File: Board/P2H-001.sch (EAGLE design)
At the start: 26 parts, among them IC1 LTC485N, IC2 74LS07N, IC3 74LS157N, IC4 LTC485N, IC5 TLC5941NT, U1 ARDUINO_PRO_MINI

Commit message: Brush up.
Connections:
- net GND: now also CN2.4
- net VCC: now also CN2.1; no longer CN2.4
- net VDD: no longer CN2.1
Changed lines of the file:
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@@
 <part name="SUPPLY32" library="supply2" deviceset="VCC" device=""/>
 <part name="JP1" library="pinhead" deviceset="PINHD-1X2" device=""/>
-<part name="VDD1" library="supply1" deviceset="VDD" device=""/>
 <part name="SUPPLY15" library="supply2" deviceset="VCC" device=""/>
 <part name="SUPPLY13" library="supply2" deviceset="GND" device=""/>
@@
 <instance part="SUPPLY32" gate="G$1" x="243.84" y="-50.8"/>
 <instance part="JP1" gate="G$1" x="33.02" y="-38.1"/>
-<instance part="VDD1" gate="G$1" x="27.94" y="134.62"/>
 <instance part="SUPPLY15" gate="G$1" x="167.64" y="127"/>
 <instance part="SUPPLY13" gate="GND" x="147.32" y="-22.86"/>
@@
 <pinref part="CN2" gate="G$1" pin="2"/>
 <pinref part="CN2" gate="G$1" pin="3"/>
+<pinref part="CN2" gate="G$1" pin="4"/>
+<wire x1="5.08" y1="38.1" x2="12.7" y2="38.1" width="0.1524" layer="91"/>
+<wire x1="12.7" y1="38.1" x2="12.7" y2="35.56" width="0.1524" layer="91"/>
+<junction x="12.7" y="35.56"/>
 </segment>
 <segment>
@@
 <segment>
 <pinref part="SUPPLY2" gate="G$1" pin="VCC"/>
-<wire x1="25.4" y1="38.1" x2="25.4" y2="124.46" width="0.1524" layer="91"/>
-<wire x1="25.4" y1="38.1" x2="5.08" y2="38.1" width="0.1524" layer="91"/>
-<pinref part="CN2" gate="G$1" pin="4"/>
+<wire x1="25.4" y1="30.48" x2="25.4" y2="124.46" width="0.1524" layer="91"/>
+<pinref part="CN2" gate="G$1" pin="1"/>
+<wire x1="25.4" y1="30.48" x2="5.08" y2="30.48" width="0.1524" layer="91"/>
 </segment>
 <segment>
@@
 <wire x1="254" y1="15.24" x2="261.62" y2="15.24" width="0.1524" layer="91"/>
 <pinref part="SV2" gate="G$1" pin="6"/>
+<label x="218.44" y="-7.62" size="1.778" layer="95"/>
 </segment>
 </net>
@@
 <wire x1="251.46" y1="17.78" x2="251.46" y2="-10.16" width="0.1524" layer="91"/>
 <pinref part="SV2" gate="G$1" pin="8"/>
+<label x="218.44" y="-10.16" size="1.778" layer="95"/>
 </segment>
 </net>
@@
 <wire x1="284.48" y1="15.24" x2="276.86" y2="15.24" width="0.1524" layer="91"/>
 <pinref part="SV2" gate="G$1" pin="5"/>
+<label x="218.44" y="-15.24" size="1.778" layer="95"/>
 </segment>
 </net>
@@
 <wire x1="256.54" y1="12.7" x2="256.54" y2="-2.54" width="0.1524" layer="91"/>
 <pinref part="SV2" gate="G$1" pin="4"/>
+<label x="218.44" y="-2.54" size="1.778" layer="95"/>
 </segment>
 </net>
@@
 <wire x1="281.94" y1="12.7" x2="276.86" y2="12.7" width="0.1524" layer="91"/>
 <pinref part="SV2" gate="G$1" pin="3"/>
+<label x="218.44" y="-5.08" size="1.778" layer="95"/>
 </segment>
 </net>
@@
 <wire x1="116.84" y1="45.72" x2="116.84" y2="132.08" width="0.1524" layer="91"/>
 <pinref part="U1" gate="G$1" pin="RAW"/>
-</segment>
-<segment>
-<pinref part="VDD1" gate="G$1" pin="VDD"/>
-<wire x1="27.94" y1="132.08" x2="27.94" y2="30.48" width="0.1524" layer="91"/>
-<wire x1="27.94" y1="30.48" x2="5.08" y2="30.48" width="0.1524" layer="91"/>
-<pinref part="CN2" gate="G$1" pin="1"/>
 </segment>
 <segment>
@@
 <wire x1="287.02" y1="17.78" x2="276.86" y2="17.78" width="0.1524" layer="91"/>
 <pinref part="SV2" gate="G$1" pin="7"/>
-</segment>
-</net>
+<label x="218.44" y="-12.7" size="1.778" layer="95"/>
+</segment>
+</net>

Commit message: Hotfix.
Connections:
- new net N$10: IC5.SOUT, SV2.3
- net SIN: no longer SV2.3
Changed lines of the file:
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@@
 <wire x1="114.3" y1="20.32" x2="109.22" y2="20.32" width="0.1524" layer="91"/>
 <label x="111.76" y="20.32" size="1.778" layer="95"/>
-<wire x1="215.9" y1="-5.08" x2="281.94" y2="-5.08" width="0.1524" layer="91"/>
-<junction x="215.9" y="-5.08"/>
 <pinref part="U1" gate="G$1" pin="*11"/>
-<wire x1="281.94" y1="-5.08" x2="281.94" y2="12.7" width="0.1524" layer="91"/>
-<wire x1="281.94" y1="12.7" x2="276.86" y2="12.7" width="0.1524" layer="91"/>
-<pinref part="SV2" gate="G$1" pin="3"/>
 <label x="218.44" y="-5.08" size="1.778" layer="95"/>
 </segment>
@@
 </segment>
 </net>
+<net name="N$10" class="0">
+<segment>
+<pinref part="SV2" gate="G$1" pin="3"/>
+<wire x1="281.94" y1="12.7" x2="276.86" y2="12.7" width="0.1524" layer="91"/>
+<pinref part="IC5" gate="G$1" pin="SOUT"/>
+<wire x1="218.44" y1="7.62" x2="218.44" y2="2.54" width="0.1524" layer="91"/>
+<wire x1="218.44" y1="2.54" x2="281.94" y2="2.54" width="0.1524" layer="91"/>
+<wire x1="281.94" y1="2.54" x2="281.94" y2="12.7" width="0.1524" layer="91"/>
+</segment>
+</net>

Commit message: Board and Doc update.
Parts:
- added JP2: (no value), pinhead:PINHD-1X2
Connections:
- net MIDIRX: now also JP2.2
- net N$1: now also JP2.1
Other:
- moved on the sheet: JP1
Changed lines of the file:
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@@
 <part name="VDD5" library="supply1" deviceset="VDD" device=""/>
 <part name="SV2" library="con-ml" deviceset="ML10" device=""/>
+<part name="JP2" library="pinhead" deviceset="PINHD-1X2" device=""/>
 </parts>
 <sheets>
@@
 <instance part="SUPPLY29" gate="G$1" x="236.22" y="-50.8"/>
 <instance part="SUPPLY32" gate="G$1" x="243.84" y="-50.8"/>
-<instance part="JP1" gate="G$1" x="33.02" y="-38.1"/>
+<instance part="JP1" gate="G$1" x="40.64" y="-12.7"/>
 <instance part="SUPPLY15" gate="G$1" x="167.64" y="127"/>
 <instance part="SUPPLY13" gate="GND" x="147.32" y="-22.86"/>
@@
 <instance part="VDD5" gate="G$1" x="281.94" y="33.02"/>
 <instance part="SV2" gate="G$1" x="269.24" y="15.24"/>
+<instance part="JP2" gate="G$1" x="88.9" y="-30.48"/>
 </instances>
 <busses>
@@
 <label x="116.84" y="-60.96" size="1.778" layer="95"/>
 <pinref part="IC3" gate="A" pin="1A"/>
-<wire x1="58.42" y1="-60.96" x2="152.4" y2="-60.96" width="0.1524" layer="91"/>
+<wire x1="58.42" y1="-60.96" x2="78.74" y2="-60.96" width="0.1524" layer="91"/>
+<pinref part="JP2" gate="G$1" pin="2"/>
+<wire x1="78.74" y1="-60.96" x2="152.4" y2="-60.96" width="0.1524" layer="91"/>
+<wire x1="86.36" y1="-30.48" x2="78.74" y2="-30.48" width="0.1524" layer="91"/>
+<wire x1="78.74" y1="-30.48" x2="78.74" y2="-60.96" width="0.1524" layer="91"/>
+<junction x="78.74" y="-60.96"/>
 </segment>
 </net>
@@
 <net name="RX" class="0">
 <segment>
-<pinref part="JP1" gate="G$1" pin="1"/>
-<wire x1="30.48" y1="-35.56" x2="30.48" y2="43.18" width="0.1524" layer="91"/>
 <wire x1="30.48" y1="43.18" x2="86.36" y2="43.18" width="0.1524" layer="91"/>
 <label x="76.2" y="43.18" size="1.778" layer="95"/>
 <pinref part="U1" gate="G$1" pin="RXI"/>
+<pinref part="JP1" gate="G$1" pin="1"/>
+<wire x1="30.48" y1="43.18" x2="30.48" y2="-10.16" width="0.1524" layer="91"/>
+<wire x1="30.48" y1="-10.16" x2="38.1" y2="-10.16" width="0.1524" layer="91"/>
 </segment>
 </net>
@@
 <segment>
 <pinref part="JP1" gate="G$1" pin="2"/>
-<wire x1="30.48" y1="-38.1" x2="30.48" y2="-60.96" width="0.1524" layer="91"/>
+<wire x1="38.1" y1="-12.7" x2="30.48" y2="-12.7" width="0.1524" layer="91"/>
+<wire x1="30.48" y1="-12.7" x2="30.48" y2="-27.94" width="0.1524" layer="91"/>
 <pinref part="IC3" gate="A" pin="1Y"/>
+<wire x1="30.48" y1="-27.94" x2="30.48" y2="-60.96" width="0.1524" layer="91"/>
 <wire x1="33.02" y1="-60.96" x2="30.48" y2="-60.96" width="0.1524" layer="91"/>
-</segment>
-</net>
+<pinref part="JP2" gate="G$1" pin="1"/>
+<wire x1="86.36" y1="-27.94" x2="30.48" y2="-27.94" width="0.1524" layer="91"/>
+<junction x="30.48" y="-27.94"/>
+</segment>
+</net>

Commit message: Jumper to Switch.
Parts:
- removed JP1, JP2: (no value), pinhead:PINHD-1X2
- added S1: TL39PO, switch:TL39PO
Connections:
- net MIDIRX: now also S1.O; no longer JP2.2
- net N$1: now also S1.S; no longer JP1.2, JP2.1
- net RX: now also S1.P; no longer JP1.1
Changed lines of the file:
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@@
 <part name="SUPPLY29" library="supply2" deviceset="VCC" device=""/>
 <part name="SUPPLY32" library="supply2" deviceset="VCC" device=""/>
-<part name="JP1" library="pinhead" deviceset="PINHD-1X2" device=""/>
 <part name="SUPPLY15" library="supply2" deviceset="VCC" device=""/>
 <part name="SUPPLY13" library="supply2" deviceset="GND" device=""/>
@@
 <part name="VDD5" library="supply1" deviceset="VDD" device=""/>
 <part name="SV2" library="con-ml" deviceset="ML10" device=""/>
-<part name="JP2" library="pinhead" deviceset="PINHD-1X2" device=""/>
+<part name="S1" library="switch" deviceset="TL39PO" device=""/>
 </parts>
 <sheets>
@@
 <instance part="SUPPLY29" gate="G$1" x="236.22" y="-50.8"/>
 <instance part="SUPPLY32" gate="G$1" x="243.84" y="-50.8"/>
-<instance part="JP1" gate="G$1" x="40.64" y="-12.7"/>
 <instance part="SUPPLY15" gate="G$1" x="167.64" y="127"/>
 <instance part="SUPPLY13" gate="GND" x="147.32" y="-22.86"/>
@@
 <instance part="VDD5" gate="G$1" x="281.94" y="33.02"/>
 <instance part="SV2" gate="G$1" x="269.24" y="15.24"/>
-<instance part="JP2" gate="G$1" x="88.9" y="-30.48"/>
+<instance part="S1" gate="BEF1" x="33.02" y="-7.62" rot="R180"/>
 </instances>
 <busses>
@@
 <pinref part="IC3" gate="A" pin="1A"/>
 <wire x1="58.42" y1="-60.96" x2="78.74" y2="-60.96" width="0.1524" layer="91"/>
-<pinref part="JP2" gate="G$1" pin="2"/>
 <wire x1="78.74" y1="-60.96" x2="152.4" y2="-60.96" width="0.1524" layer="91"/>
-<wire x1="86.36" y1="-30.48" x2="78.74" y2="-30.48" width="0.1524" layer="91"/>
 <wire x1="78.74" y1="-30.48" x2="78.74" y2="-60.96" width="0.1524" layer="91"/>
 <junction x="78.74" y="-60.96"/>
+<pinref part="S1" gate="BEF1" pin="O"/>
+<wire x1="35.56" y1="-12.7" x2="35.56" y2="-30.48" width="0.1524" layer="91"/>
+<wire x1="35.56" y1="-30.48" x2="78.74" y2="-30.48" width="0.1524" layer="91"/>
+<label x="35.56" y="-22.86" size="1.778" layer="95"/>
 </segment>
 </net>
@@
 <net name="RX" class="0">
 <segment>
-<wire x1="30.48" y1="43.18" x2="86.36" y2="43.18" width="0.1524" layer="91"/>
 <label x="76.2" y="43.18" size="1.778" layer="95"/>
 <pinref part="U1" gate="G$1" pin="RXI"/>
-<pinref part="JP1" gate="G$1" pin="1"/>
-<wire x1="30.48" y1="43.18" x2="30.48" y2="-10.16" width="0.1524" layer="91"/>
-<wire x1="30.48" y1="-10.16" x2="38.1" y2="-10.16" width="0.1524" layer="91"/>
+<pinref part="S1" gate="BEF1" pin="P"/>
+<wire x1="33.02" y1="43.18" x2="86.36" y2="43.18" width="0.1524" layer="91"/>
+<wire x1="33.02" y1="-2.54" x2="33.02" y2="43.18" width="0.1524" layer="91"/>
 </segment>
 </net>
@@
 <net name="N$1" class="0">
 <segment>
-<pinref part="JP1" gate="G$1" pin="2"/>
-<wire x1="38.1" y1="-12.7" x2="30.48" y2="-12.7" width="0.1524" layer="91"/>
-<wire x1="30.48" y1="-12.7" x2="30.48" y2="-27.94" width="0.1524" layer="91"/>
 <pinref part="IC3" gate="A" pin="1Y"/>
-<wire x1="30.48" y1="-27.94" x2="30.48" y2="-60.96" width="0.1524" layer="91"/>
+<wire x1="30.48" y1="-12.7" x2="30.48" y2="-60.96" width="0.1524" layer="91"/>
 <wire x1="33.02" y1="-60.96" x2="30.48" y2="-60.96" width="0.1524" layer="91"/>
-<pinref part="JP2" gate="G$1" pin="1"/>
-<wire x1="86.36" y1="-27.94" x2="30.48" y2="-27.94" width="0.1524" layer="91"/>
-<junction x="30.48" y="-27.94"/>
-</segment>
-</net>
+<pinref part="S1" gate="BEF1" pin="S"/>
+</segment>
+</net>

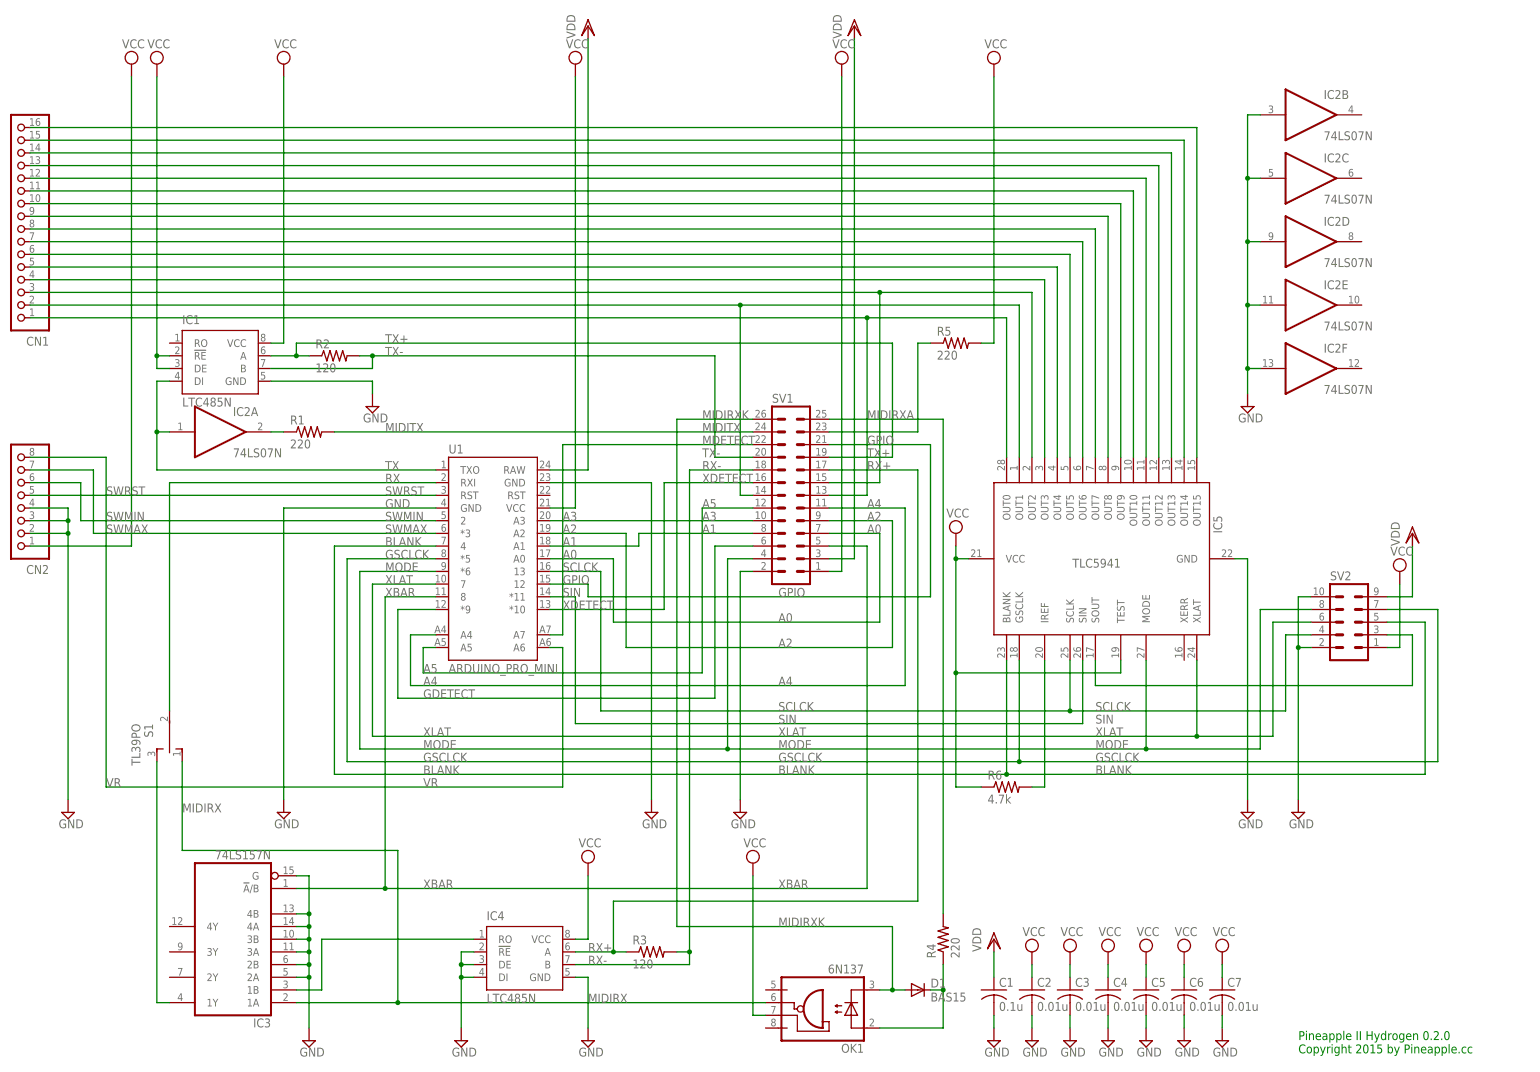
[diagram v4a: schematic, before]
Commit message: changed circuit of mdetect.
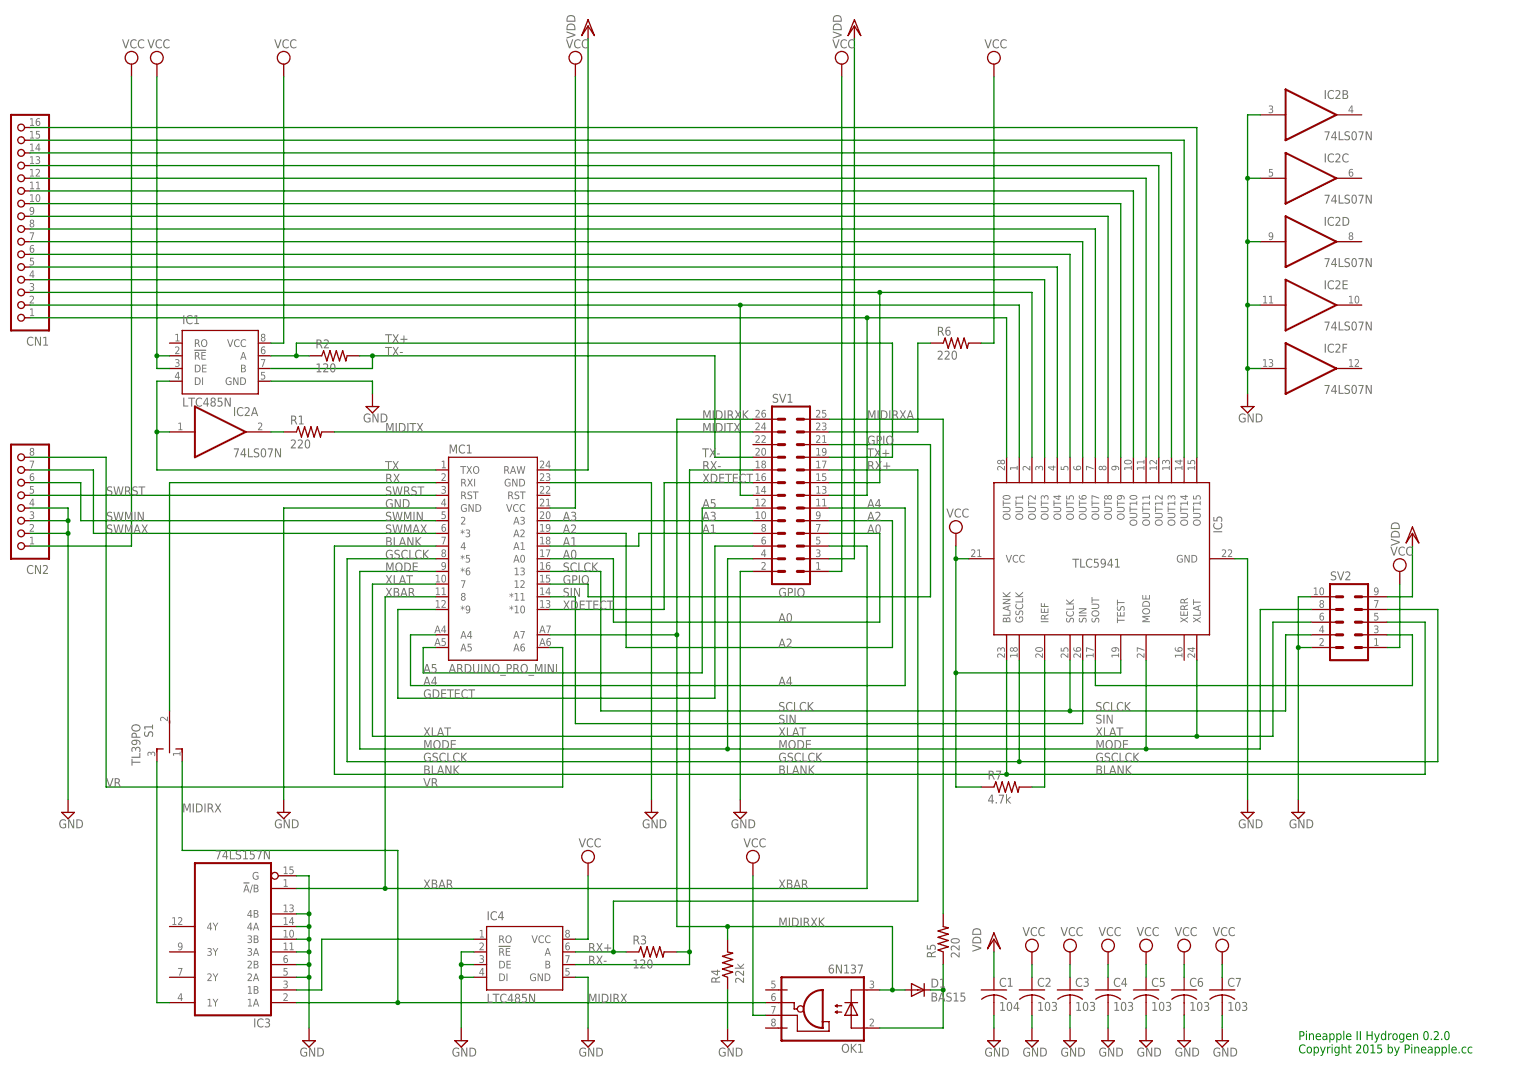
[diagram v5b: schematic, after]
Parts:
- added R7: 4.7k, resistor:R-US_0204/5
- C1: value 0.1u -> 104
- C2, C3, C4, C5, C6, C7: value 0.01u -> 103
- R4: value 220 -> 22k
- R6: value 4.7k -> 220
- renumbered U1 to MC1
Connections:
- removed net MDETECT: MC1.A7, SV1.22
- net GND: now also R4.1
- net MIDIRXA: now also R5.2; no longer R4.2
- net MIDIRXK: now also MC1.A7, R4.2
- net N$13: now also R5.1; no longer R4.1
- net N$37: now also R7.2; no longer R6.2
- net N$4: now also R6.1; no longer R5.1
- net VCC: now also R6.2, R7.1; no longer R5.2, R6.1
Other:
- moved on the sheet: R4, R5, R6

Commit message: changed detector cicuits for midi in and out.
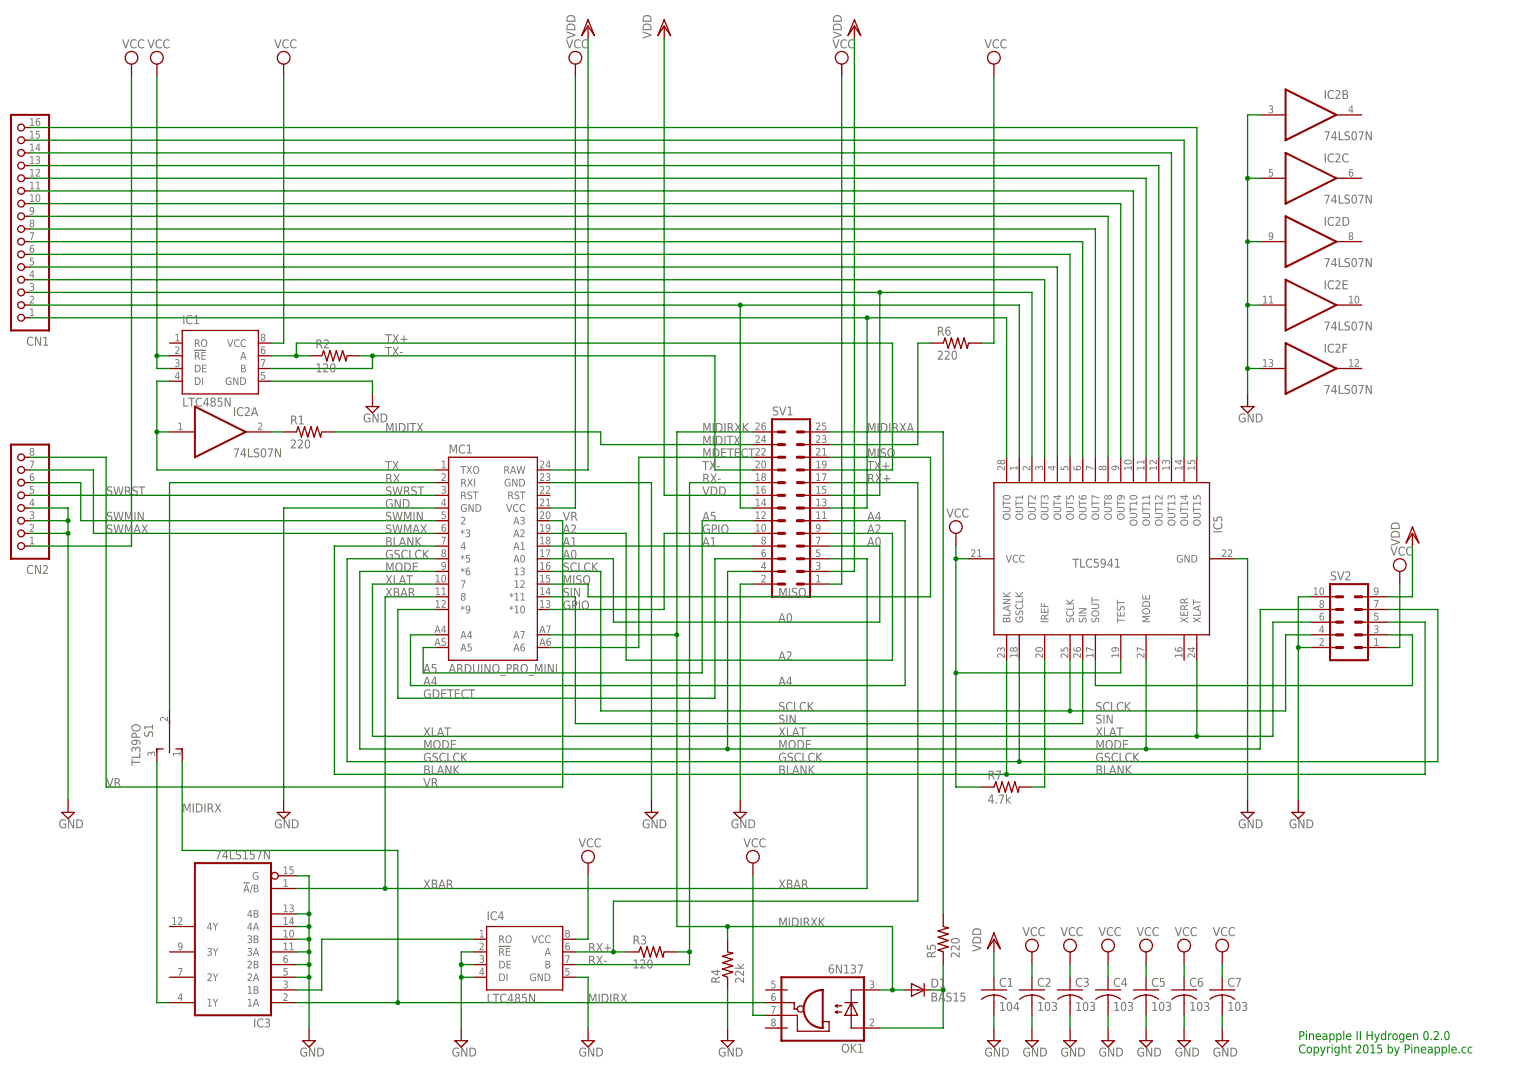
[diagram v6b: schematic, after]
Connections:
- removed net A3: MC1.A3, SV1.10
- removed net XDETECT: MC1.*10, SV1.16
- new net MDETECT: MC1.A6, SV1.22
- new net MISO: MC1.12, SV1.21
- net GPIO: now also MC1.*10, SV1.10; no longer MC1.12, SV1.21
- net VDD: now also SV1.16
- net VR: now also MC1.A3; no longer MC1.A6
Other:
- moved on the sheet: SV1
